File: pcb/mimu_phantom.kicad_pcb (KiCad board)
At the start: 2 copper layers, 50 x 27 mm, 34 parts, among them J1 OPT, SW1 SW_Push, U1 AQY211EH, U2 ATTINY88AU, U3 MCP16331CH, U4 H11F1M

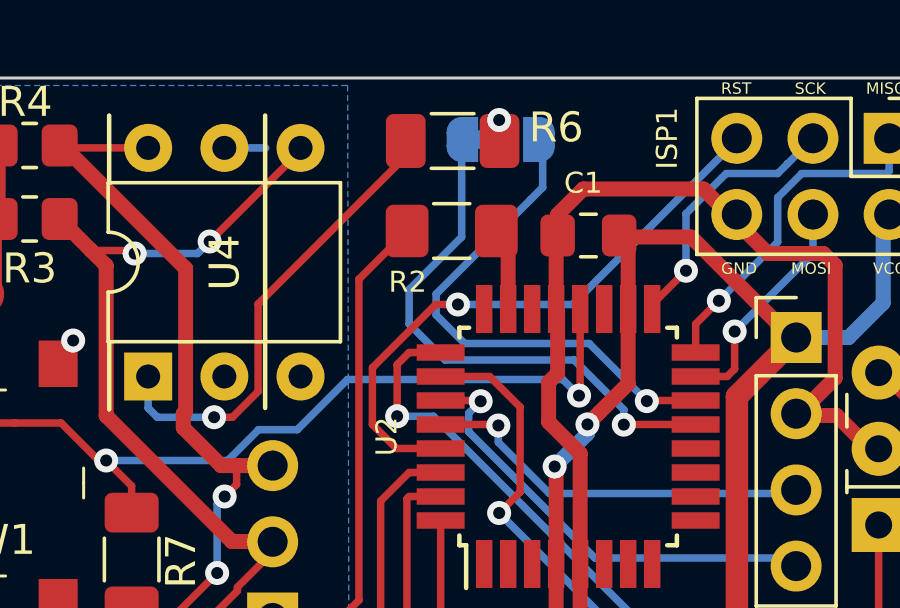
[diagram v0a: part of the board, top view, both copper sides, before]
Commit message: Bugfix: Added missing filter cap on PWM output
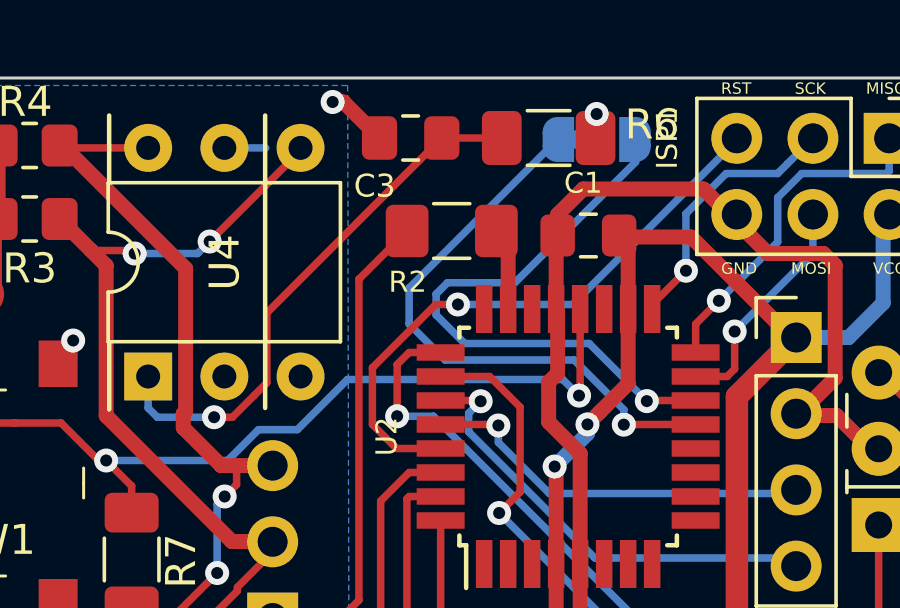
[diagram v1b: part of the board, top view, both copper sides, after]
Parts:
- added C3: 47nF, Capacitor_SMD:C_0805_2012Metric_Pad1.18x1.45mm_HandSolder, F.Cu at (132.0, 75.0)
- moved R6 3.20 mm to (136.6, 75.0)
- moved SW2 3.20 mm to (138.2, 75.0)
- renumbered PWM to SW2
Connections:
- U2 pad 1: (no net) -> Net-(U2-Pad1)
- U2 pad 10: (no net) -> Net-(U2-Pad10)
- U2 pad 11: (no net) -> Net-(U2-Pad11)
- U2 pad 12: (no net) -> Net-(U2-Pad12)
- U2 pad 19: (no net) -> Net-(U2-Pad19)
- U2 pad 2: (no net) -> Net-(U2-Pad2)
- U2 pad 22: (no net) -> Net-(U2-Pad22)
- U2 pad 24: (no net) -> Net-(U2-Pad24)
- U2 pad 3: (no net) -> Net-(U2-Pad3)
- U2 pad 6: (no net) -> Net-(U2-Pad6)
- U2 pad 7: (no net) -> Net-(U2-Pad7)
- U2 pad 8: (no net) -> Net-(U2-Pad8)
- U2 pad 9: (no net) -> Net-(U2-Pad9)
- U3 pad 4: (no net) -> Net-(U3-Pad4)
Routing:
- net Net-(C3-Pad1): track 14.9 -> 18.2 mm
- net OC1B: track 17.0 -> 19.8 mm
- net XLR_GND: track 66.5 -> 68.6 mm, vias 18 -> 19
- net OC1A: track 18.4 -> 19.7 mm

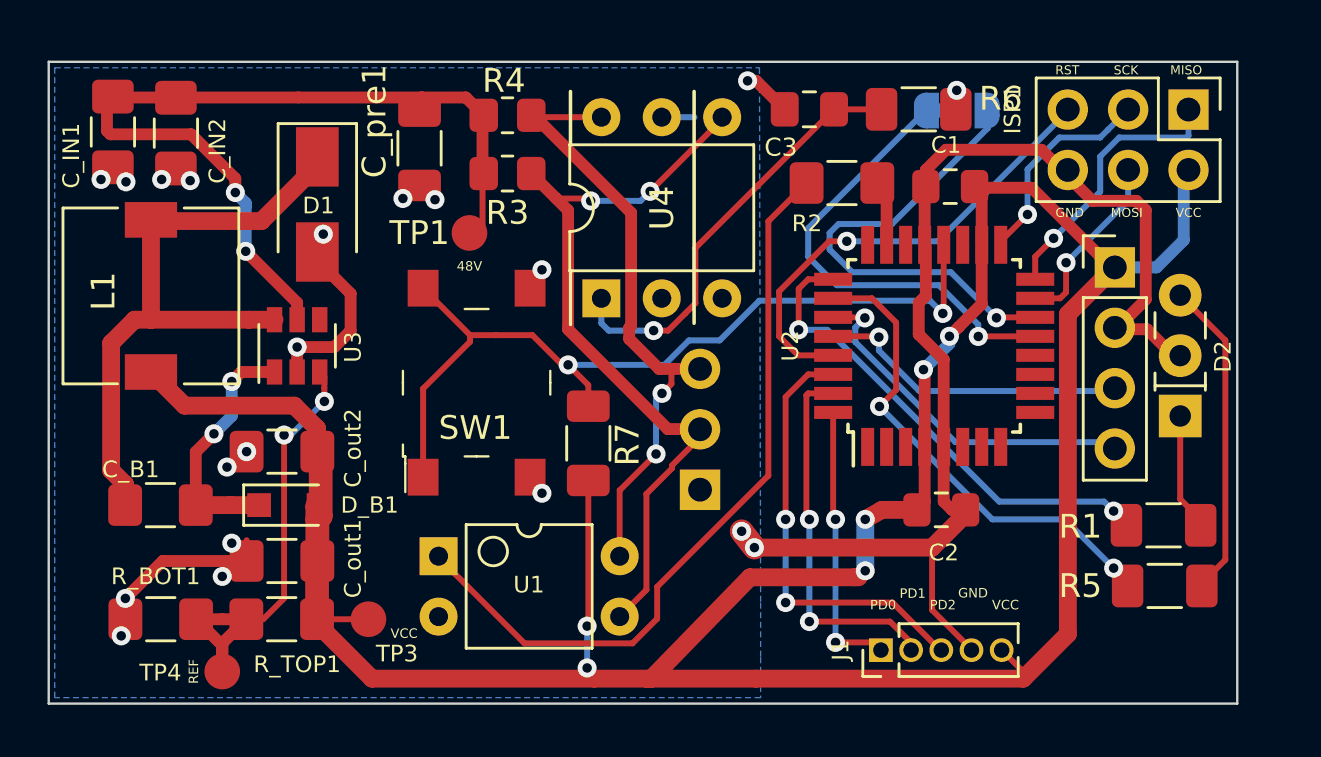
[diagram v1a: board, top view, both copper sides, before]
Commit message: re-structured 3D-Models so that scaling is correct
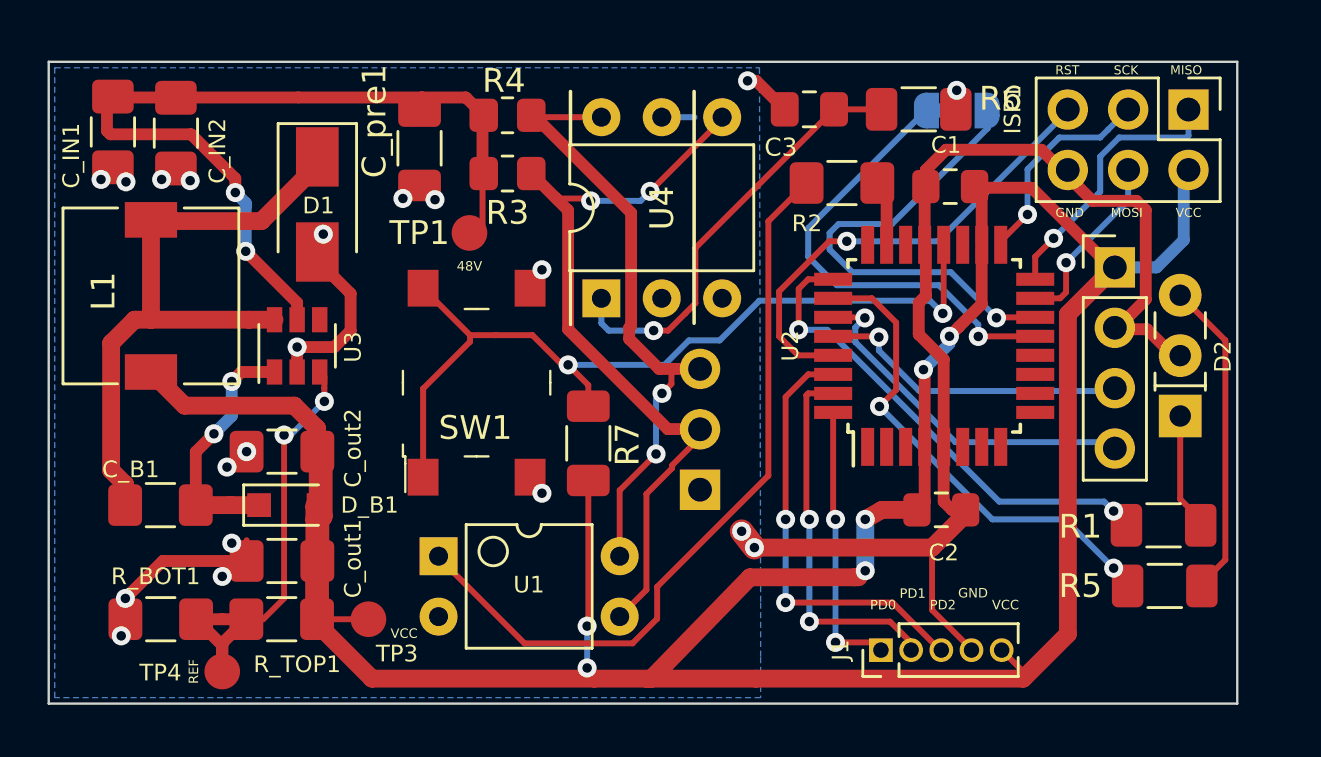
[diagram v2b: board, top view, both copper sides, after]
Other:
- net class Default removed

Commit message: First impression of new v3!
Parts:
- removed C3: 47nF, Capacitor_SMD:C_0805_2012Metric_Pad1.18x1.45mm_HandSolder
- removed R7: 1k, Capacitor_SMD:C_1206_3216Metric_Pad1.33x1.80mm_HandSolder
- removed SW2: SW_SPDT, Jumper:SolderJumper-3_P1.3mm_Bridged12_RoundedPad1.0x1.5mm_NumberLabels
- added C_pre2: 50-100uF @24V, Capacitor_SMD:C_1206_3216Metric_Pad1.33x1.80mm_HandSolder, F.Cu at (117.9, 78.8)
- added Q1: BSS84, Package_TO_SOT_SMD:SOT-23, F.Cu at (133.9, 77.1)
- C_pre1: value 100uF -> 50-100uF @24V
- D2: value LED_Dual_ACA -> LED_Dual_KAK; footprint LED_THT:LED_Rectangular_W5.0mm_H2.0mm-3Pins -> LED_THT:LED_D3.0mm-3
- ISP1: footprint Connector_PinHeader_2.54mm:PinHeader_2x03_P2.54mm_Vertical -> ProjectLibrary:PinHeader_2x03_P2.54mm_Vertical_pogo
- R2: value 1k -> 12R; footprint Resistor_SMD:R_1206_3216Metric_Pad1.42x1.75mm_HandSolder -> Resistor_SMD:R_1206_3216Metric_Pad1.30x1.75mm_HandSolder
- R6: value 100R -> 68R; footprint Capacitor_SMD:C_1206_3216Metric_Pad1.33x1.80mm_HandSolder -> Resistor_SMD:R_1206_3216Metric_Pad1.30x1.75mm_HandSolder
- U1: value AQY211EH -> PC817
- U4: value H11F1M -> AD5258; footprint Package_DIP:DIP-6_W7.62mm -> Package_SO:MSOP-10_3x3mm_P0.5mm
- moved R6 15.6 mm to (121.4, 78.6), turned to -90 degrees
- moved R4 10.9 mm to (126.8, 83.2)
- moved TP1 10.8 mm to (126.7, 74.3)
- moved R3 10.7 mm to (124.4, 87.1), turned to 90 degrees
- moved R2 9.48 mm to (123.9, 78.6), turned to 90 degrees
- moved U4 7.47 mm to (129.1, 78.3)
- moved D2 4.10 mm to (147.5, 83.8), turned to -90 degrees
- moved TP3 2.99 mm to (111.6, 98.8)
- moved C_IN1 1.61 mm to (104.0, 77.0)
- moved C_IN2 1.61 mm to (106.6, 77.0)
- moved L1 1.38 mm to (105.2, 83.9)
- moved C_pre1 1.17 mm to (115.5, 77.8)
- moved R1 1.01 mm to (145.9, 92.2)
- moved R5 1.01 mm to (146.0, 94.8)
- moved C_out1 0.91 mm to (110.7, 94.2)
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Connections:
- C_pre1 pad 2: XLR_GND -> Net-(C_pre1-Pad2)
- R2 pad 1: MUTE -> Net-(R2-Pad1)
- R2 pad 2: Net-(R2-Pad2) -> Net-(Q1-Pad3)
- R6 pad 1: ATT -> Net-(Q1-Pad3)
- R6 pad 2: Net-(C3-Pad1) -> Net-(U1-Pad1)
- U1 pad 1: Net-(R2-Pad2) -> Net-(U1-Pad1)
- U2 pad 1: Net-(U2-Pad1) -> unconnected-(U2-Pad1)
- U2 pad 10: Net-(U2-Pad10) -> unconnected-(U2-Pad10)
- U2 pad 11: Net-(U2-Pad11) -> unconnected-(U2-Pad11)
- U2 pad 12: Net-(U2-Pad12) -> unconnected-(U2-Pad12)
- U2 pad 13: OC1A -> unconnected-(U2-Pad13)
- U2 pad 14: OC1B -> unconnected-(U2-Pad14)
- U2 pad 19: Net-(U2-Pad19) -> unconnected-(U2-Pad19)
- U2 pad 2: Net-(U2-Pad2) -> unconnected-(U2-Pad2)
- U2 pad 22: Net-(U2-Pad22) -> unconnected-(U2-Pad22)
- U2 pad 23: MUTE -> MUTE_DRIVE
- U2 pad 24: Net-(U2-Pad24) -> unconnected-(U2-Pad24)
- U2 pad 3: Net-(U2-Pad3) -> unconnected-(U2-Pad3)
- U2 pad 6: Net-(U2-Pad6) -> unconnected-(U2-Pad6)
- U2 pad 7: Net-(U2-Pad7) -> unconnected-(U2-Pad7)
- U2 pad 8: Net-(U2-Pad8) -> unconnected-(U2-Pad8)
- U2 pad 9: Net-(U2-Pad9) -> unconnected-(U2-Pad9)
- U3 pad 4: Net-(U3-Pad4) -> unconnected-(U3-Pad4)
- U4 pad 1: Net-(C3-Pad1) -> Net-(R2-Pad1)
- U4 pad 3: (no net) -> XLR_GND
- U4 pad 4: XLR_HOT -> SDA
- U4 pad 5: (no net) -> SCL
- U4 pad 6: XLR_COLD -> VCC
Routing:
- net Net-(R2-Pad2): track 32.1 -> 0.00 mm
- net XLR_HOT: track 32.2 -> 12.3 mm, vias 2 -> 0
- net OC1B: track 19.8 -> 0.00 mm, vias 1 -> 0
- net OC1A: track 19.7 -> 0.00 mm, vias 1 -> 0
- net Net-(C3-Pad1): track 18.2 -> 0.00 mm, vias 1 -> 0
- net Net-(U1-Pad1): track 0.00 -> 17.6 mm
- net Net-(Q1-Pad3): track 0.00 -> 17.1 mm, vias 0 -> 2
- net XLR_COLD: track 26.0 -> 12.9 mm
- net +BATT: track 36.2 -> 46.8 mm
- net SDA: track 14.4 -> 22.4 mm, vias 1 -> 2
- net Net-(R5-Pad2): track 12.8 -> 5.33 mm, vias 0 -> 1
- net SCL: track 12.7 -> 19.1 mm
- net VCC: track 120.8 -> 127.0 mm, vias 6 -> 7
- net Net-(R1-Pad2): track 4.49 -> 9.56 mm
- net Net-(R2-Pad1): track 0.00 -> 4.34 mm, vias 0 -> 2
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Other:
- board text added: "MIMU Phantom v3 PP 12.22"
- board text removed: "MIMU Phantom v2 PP 10.21"

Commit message: First layout
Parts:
- added C3: 50-100uF, Capacitor_THT:CP_Radial_D4.0mm_P2.00mm, F.Cu at (127.7, 96.4)
- C1, C2: footprint Capacitor_SMD:C_0805_2012Metric_Pad1.15x1.40mm_HandSolder -> Capacitor_SMD:C_1206_3216Metric_Pad1.33x1.80mm_HandSolder
- C_pre1, C_pre2: value 50-100uF @24V -> 3-4uF @24V
- R3, R4: footprint Resistor_SMD:R_0805_2012Metric_Pad1.20x1.40mm_HandSolder -> Resistor_SMD:R_1206_3216Metric_Pad1.30x1.75mm_HandSolder
- moved R2 3.09 mm to (142.9, 94.8)
- moved R1 3.04 mm to (142.9, 92.3)
- moved C_pre2 2.37 mm to (118.6, 76.5), turned to -90 degrees
- moved C_pre1 1.36 mm to (115.9, 76.5)
- moved R4 1.04 mm to (125.8, 82.9)
- moved C1 0.58 mm to (138.5, 78.2)
- moved C_IN2 0.51 mm to (106.6, 76.5)
- moved C_IN1 0.46 mm to (104.0, 76.5)
- moved R3 0.41 mm to (124.0, 87.0)
- moved C2 0.16 mm to (137.4, 91.9)
- renumbered R5 to R2, R2 to R5
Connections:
- C_pre1 pad 2: Net-(C_pre1-Pad2) -> XLR_GND
- C_pre2 pad 1: Net-(C_pre1-Pad2) -> +BATT
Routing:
- net XLR_GND: track 72.5 -> 114.9 mm, vias 19 -> 24
- net +BATT: track 46.8 -> 53.4 mm
- net LED_R: track 21.7 -> 17.1 mm, vias 4 -> 2
- net LED_G: track 19.9 -> 16.9 mm
- net Net-(C_pre1-Pad2): track 2.80 -> 0.00 mm
- net BUTT: track 34.3 -> 32.3 mm
- net Net-(D2-Pad3): track 5.33 -> 7.13 mm, vias 1 -> 0
- net VCC: track 127.0 -> 125.2 mm, vias 7 -> 6
- net Net-(D2-Pad1): track 9.56 -> 10.3 mm, vias 0 -> 1
- net Net-(Q1-Pad3): track 17.1 -> 16.3 mm
- net SDA: track 22.4 -> 23.0 mm, vias 2 -> 1
- net XLR_COLD: track 12.9 -> 12.3 mm, vias 2 -> 1

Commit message: Minor PCB updates
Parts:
- C3: footprint Capacitor_THT:CP_Radial_D4.0mm_P2.00mm -> Capacitor_THT:CP_Radial_D5.0mm_P2.00mm
- C_IN1, C_IN2: value 10uF -> 10uF @ 24v
- R2: footprint Capacitor_SMD:C_1206_3216Metric_Pad1.33x1.80mm_HandSolder -> Resistor_SMD:R_1206_3216Metric_Pad1.30x1.75mm_HandSolder
- moved C3 0.77 mm to (128.3, 96.9)
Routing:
- net XLR_GND: track 114.9 -> 119.5 mm
- net VCC: track 125.2 -> 122.7 mm
- net +BATT: track 53.4 -> 54.0 mm
